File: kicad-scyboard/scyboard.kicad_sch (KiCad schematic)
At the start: 45 parts, among them U1 Nice_Nano_V2

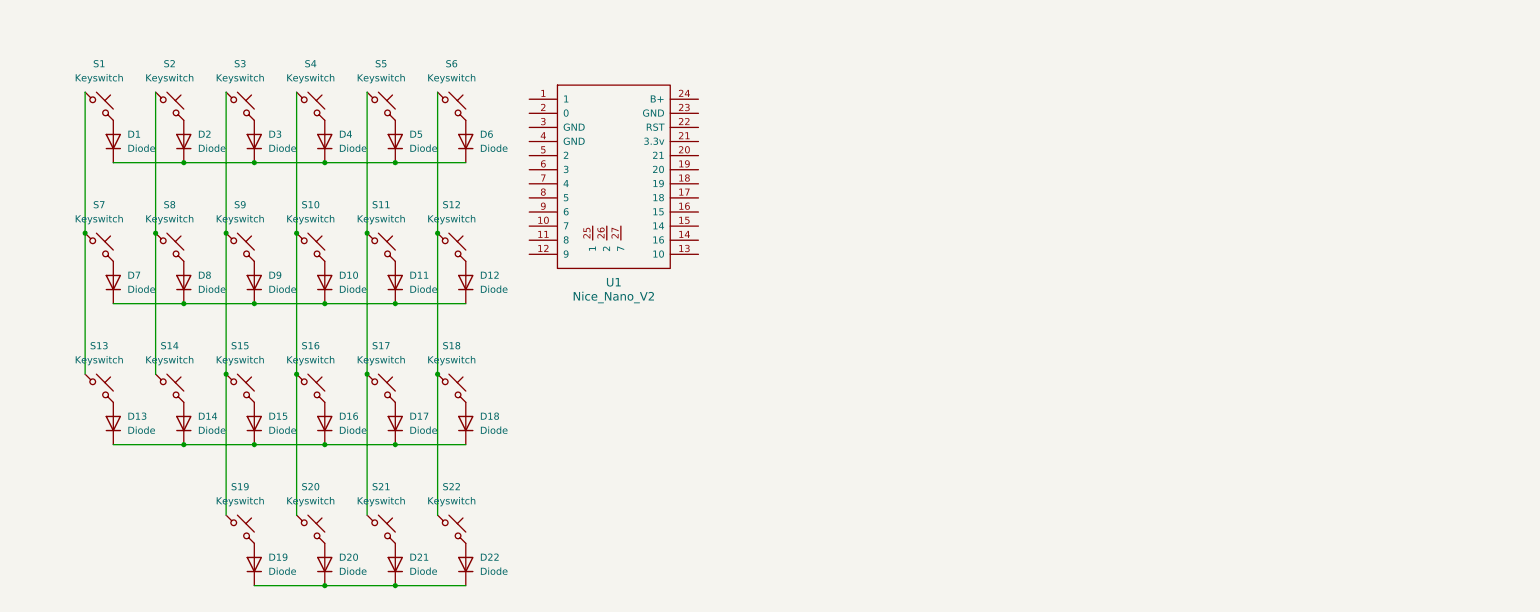
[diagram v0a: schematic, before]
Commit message: Update kicad
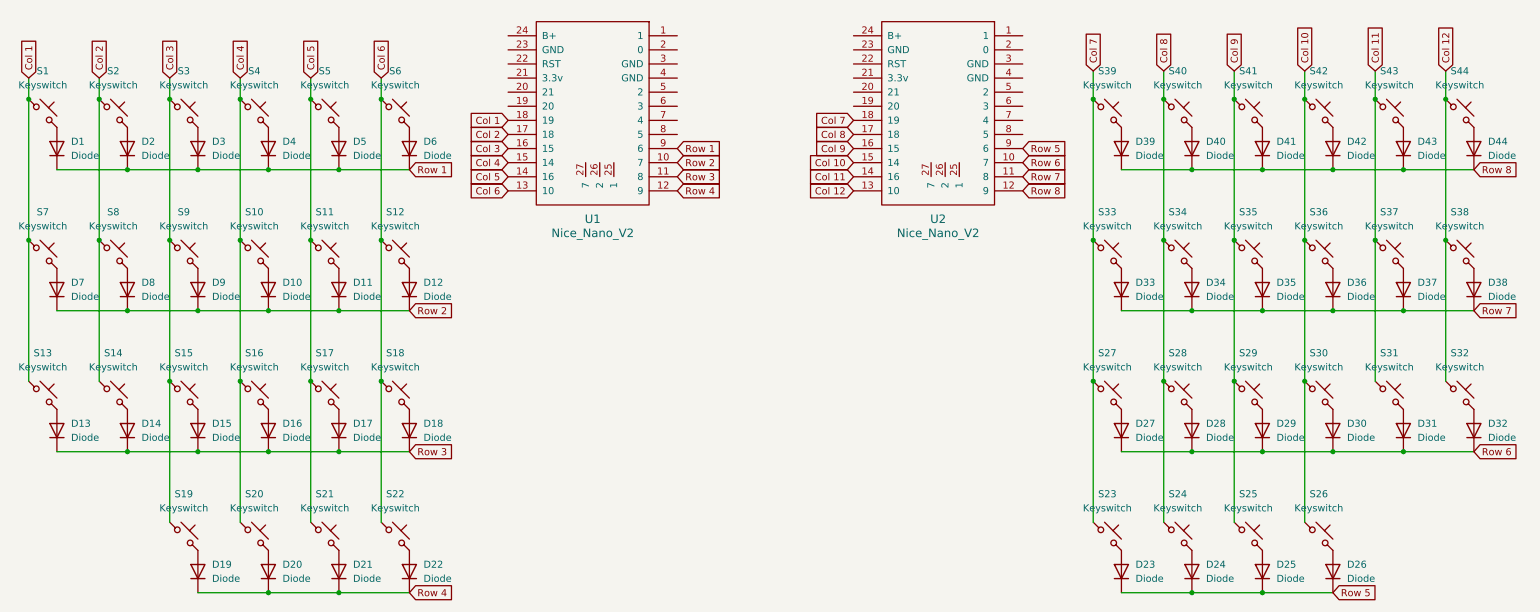
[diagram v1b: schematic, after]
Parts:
- added D23, D24, D25, D26, D27, D28, D29, D30, D31, D32, D33, D34, D35, D36, D37, D38, D39, D40, D41, D42, D43, D44: Diode, ScottoKeebs_Components:Diode_DO-35, symbol ScottoKeebs:Placeholder_Diode
- added S23, S24, S25, S26, S27, S28, S29, S30, S31, S32, S33, S34, S35, S36, S37, S38, S39, S40, S41, S42, S43, S44: Keyswitch, ScottoKeebs_Hotswap:Hotswap_Choc_V1, symbol ScottoKeebs:Placeholder_Keyswitch
- added U2: Nice_Nano_V2, ScottoKeebs_MCU:Nice_Nano_V2_Flipped, symbol ScottoKeebs:MCU_Nice_Nano_V2
- D1, D10, D11, D12, D13, D14, D15, D16, D17, D18, D19, D2, D20, D21, D22, D3, D4, D5, D6, D7, D8, D9: footprint (none) -> ScottoKeebs_Components:Diode_DO-35
- S1, S10, S11, S12, S13, S14, S15, S16, S17, S18, S19, S2, S20, S21, S22, S3, S4, S5, S6, S7, S8, S9: footprint (none) -> ScottoKeebs_Hotswap:Hotswap_Choc_V1
- U1: footprint ScottoKeebs_MCU:Nice_Nano_V2 -> ScottoKeebs_MCU:Nice_Nano_V2_Flipped
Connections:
- net Col 3: now reaches S15.1, S19.1, S3.1, S9.1
- net Col 3: now also U1.16 (15)
- net Col 4: now reaches S10.1, S16.1, S20.1, S4.1
- net Col 4: now also U1.15 (14)
- net Col 1: now reaches S1.1, S13.1, S7.1
- net Col 1: now also U1.18 (19)
- net Col 6: now reaches S12.1, S18.1, S22.1, S6.1
- net Col 6: now also U1.13 (10)
- net Row 3: now reaches D13.1 (K), D14.1 (K), D15.1 (K), D16.1 (K), D17.1 (K), D18.1 (K)
- net Row 3: now also U1.11 (8)
- net Col 2: now reaches S14.1, S2.1, S8.1
- net Col 2: now also U1.17 (18)
- net Row 1: now reaches D1.1 (K), D2.1 (K), D3.1 (K), D4.1 (K), D5.1 (K), D6.1 (K)
- net Row 1: now also U1.9 (6)
- net Col 5: now reaches S11.1, S17.1, S21.1, S5.1
- net Col 5: now also U1.14 (16)
- net Row 2: now reaches D10.1 (K), D11.1 (K), D12.1 (K), D7.1 (K), D8.1 (K), D9.1 (K)
- net Row 2: now also U1.10 (7)
- net Row 4: now reaches D19.1 (K), D20.1 (K), D21.1 (K), D22.1 (K)
- net Row 4: now also U1.12 (9)
- new net: D43.2 (A), S43.2
- new net: D39.2 (A), S39.2
- new net: D44.2 (A), S44.2
- new net: D34.2 (A), S34.2
- new net: D24.2 (A), S24.2
- new net: D31.2 (A), S31.2
- new net: D26.2 (A), S26.2
- new net: D41.2 (A), S41.2
- new net: D38.2 (A), S38.2
- new net: D37.2 (A), S37.2
- new net: D35.2 (A), S35.2
- new net: D29.2 (A), S29.2
- new net: D27.2 (A), S27.2
- new net: D40.2 (A), S40.2
- new net: D28.2 (A), S28.2
- new net: D30.2 (A), S30.2
- new net: D25.2 (A), S25.2
- new net: D42.2 (A), S42.2
- new net: D33.2 (A), S33.2
- new net: D23.2 (A), S23.2
- new net: D36.2 (A), S36.2
- new net: D32.2 (A), S32.2
- new net Col 10: S26.1, S30.1, S36.1, S42.1, U2.15 (14)
- new net Col 11: S31.1, S37.1, S43.1, U2.14 (16)
- new net Col 12: S32.1, S38.1, S44.1, U2.13 (10)
- new net Col 7: S23.1, S27.1, S33.1, S39.1, U2.18 (19)
- new net Col 8: S24.1, S28.1, S34.1, S40.1, U2.17 (18)
- new net Col 9: S25.1, S29.1, S35.1, S41.1, U2.16 (15)
- new net Row 5: D23.1 (K), D24.1 (K), D25.1 (K), D26.1 (K), U2.9 (6)
- new net Row 6: D27.1 (K), D28.1 (K), D29.1 (K), D30.1 (K), D31.1 (K), D32.1 (K), U2.10 (7)
- new net Row 7: D33.1 (K), D34.1 (K), D35.1 (K), D36.1 (K), D37.1 (K), D38.1 (K), U2.11 (8)
- new net Row 8: D39.1 (K), D40.1 (K), D41.1 (K), D42.1 (K), D43.1 (K), D44.1 (K), U2.12 (9)
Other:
- moved on the sheet: D1, D10, D11, D12, D13, D14, D15, D16, D17, D18, D19, D2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

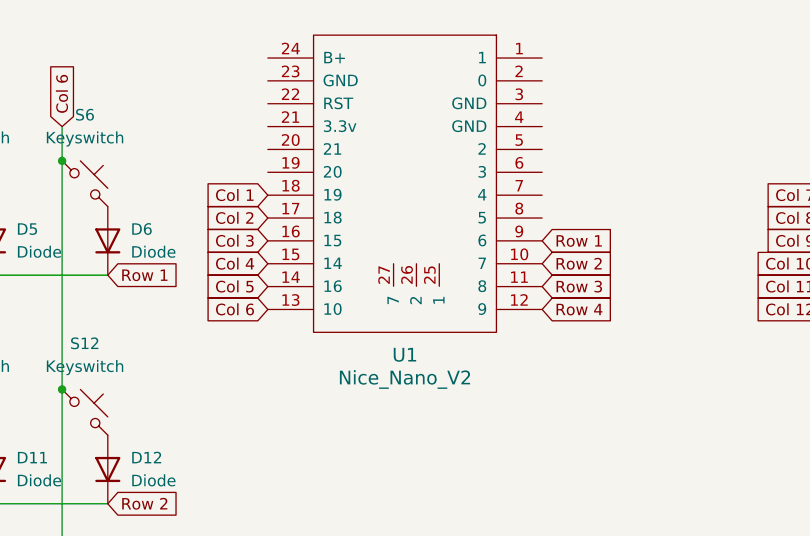
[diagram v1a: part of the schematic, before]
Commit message: Update kicad
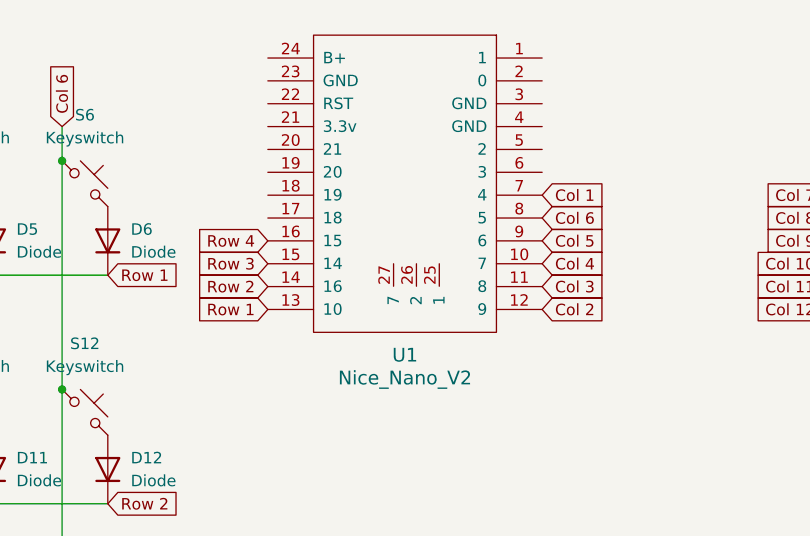
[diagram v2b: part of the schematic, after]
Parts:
- D1, D10, D11, D12, D13, D14, D15, D16, D17, D18, D19, D2, D20, D21, D22, D23, D24, D25, D26, D27, D28, D29, D3, D30, D31, D32, D33, D34, D35, D36, D37, D38, D39, D4, D40, D41, D42, D43, D44, D5, D6, D7, D8, D9: footprint ScottoKeebs_Components:Diode_DO-35 -> ScottoKeebs_Components:Diode_SOD-123
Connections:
- net Col 1: now also U1.7 (4); no longer U1.18 (19)
- net Col 2: now also U1.12 (9); no longer U1.17 (18)
- net Col 3: now also U1.11 (8); no longer U1.16 (15)
- net Col 4: now also U1.10 (7); no longer U1.15 (14)
- net Col 5: now also U1.9 (6); no longer U1.14 (16)
- net Col 6: now also U1.8 (5); no longer U1.13 (10)
- net Row 1: now also U1.13 (10); no longer U1.9 (6)
- net Row 2: now also U1.14 (16); no longer U1.10 (7)
- net Row 3: now also U1.15 (14); no longer U1.11 (8)
- net Row 4: now also U1.16 (15); no longer U1.12 (9)

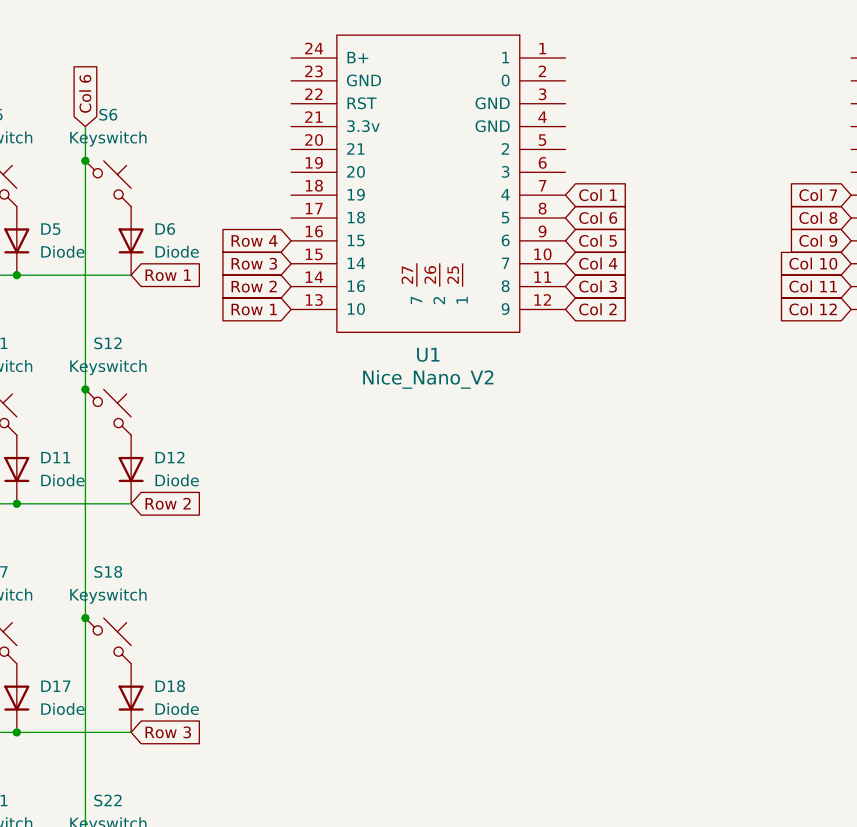
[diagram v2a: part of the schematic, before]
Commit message: Update kicad
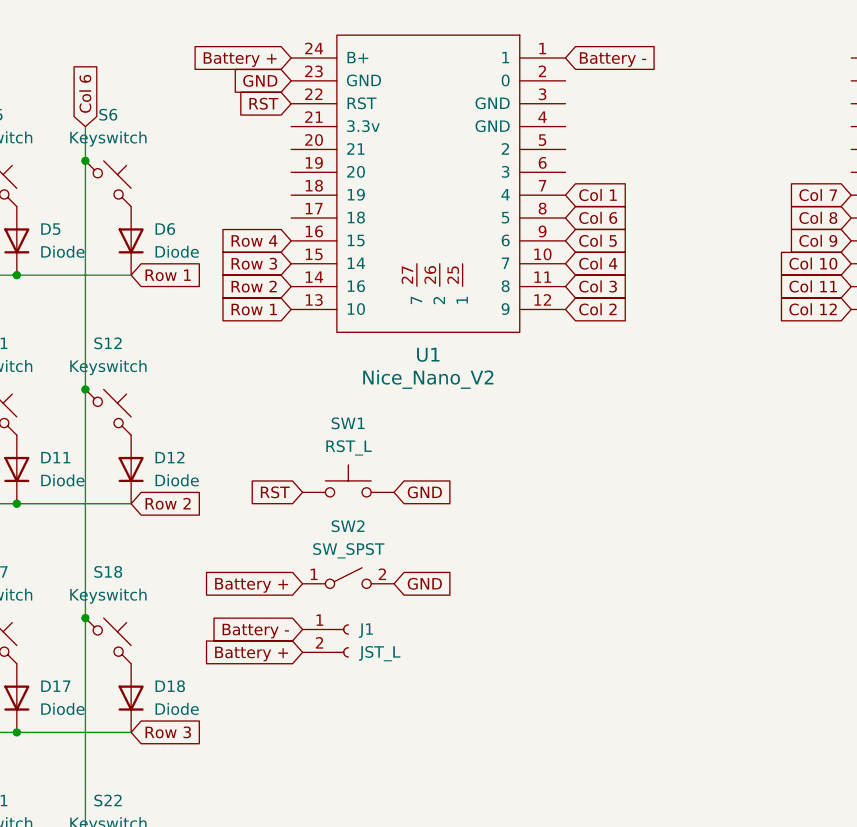
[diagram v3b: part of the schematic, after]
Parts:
- added J1: JST_L, Connector_JST:JST_PH_S2B-PH-K_1x02_P2.00mm_Horizontal, symbol Connector:Conn_01x02_Socket
- added SW1: RST_L, Button_Switch_SMD:Panasonic_EVQPUL_EVQPUC, symbol Switch:SW_Push
- added SW2: SW_SPST, symbol Switch:SW_SPST
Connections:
- net Battery -: now reaches U1.1
- net Battery -: now also J1.1 (Pin_1)
- net RST: now reaches U1.22 (RST)
- net RST: now also SW1.1
- net GND: now reaches U1.23 (GND)
- net GND: now also SW1.2, SW2.2 (B)
- net Battery +: now reaches U1.24 (B+)
- net Battery +: now also J1.2 (Pin_2), SW2.1 (A)

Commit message: Update KiCad
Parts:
- removed SW2: SW_SPST, symbol Switch:SW_SPST
- added SW2: PWR_L, Alps_Alpine_Switch_Slide:SW4_SSSS811101_ALPS, symbol Alps_Alpine:SSSS811101
- added SW3: RST_L, Button_Switch_SMD:Panasonic_EVQPUL_EVQPUC, symbol Switch:SW_Push
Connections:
- net RST_R: now reaches U2.22 (RST)
- net RST_R: now also SW3.1
- net GND_R1: now reaches U2.3 (GND)
- net GND_R1: now also SW3.2
- net VCC_L: now reaches U1.21 (3.3v)
- net GND_L1: now reaches U1.3 (GND)
- net GND_L1: now also SW1.2
- net GND_L2: now reaches U1.4 (GND)
- net GND_L2: now also SW2.3
- net Battery + renamed B+L
- net B+L: now also SW2.1
- net Battery -: no longer names the net of U1.1
- net Battery -: no longer J1.1 (Pin_1)
- net GND renamed B-L
- net B-L: now also J1.1 (Pin_1); no longer SW1.2
- net RST renamed RST_L
- new net VCC: SW2.2
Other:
- moved on the sheet: J1
